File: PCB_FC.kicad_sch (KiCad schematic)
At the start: 20 parts, among them IC1 STM32F405RGT6, IC2 ICM-42670-P, U1 BMP388, U2 AMS1117-3.3, Y1 X32258MOB4SI

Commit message: Basic design of schametic done
1. Added folder for library
2. Added USB with termination resistors
3. Added Resistor network for bootstrapping and NRST
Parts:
- removed C5, C6: 10pF, Capacitor_SMD:C_0603_1608Metric_Pad1.08x0.95mm_HandSolder, symbol Device:C
- removed C7, C8, C9: C, Capacitor_SMD:C_0603_1608Metric_Pad1.08x0.95mm_HandSolder, symbol Device:C
- added C12, C15, C16, C17, C18, C19, C20, C21: 100nf, Capacitor_SMD:C_0603_1608Metric_Pad1.08x0.95mm_HandSolder, symbol Device:C
- added C13, C14: 10uf, Capacitor_SMD:C_0603_1608Metric_Pad1.08x0.95mm_HandSolder, symbol Device:C
- added D1: LED, symbol Device:LED
- added J1: 10104111-0001LF, Footprint:10104111-0001LF, symbol 10104111-0001LF:10104111-0001LF
- added R4: 4.7k, Resistor_SMD:R_0603_1608Metric_Pad0.98x0.95mm_HandSolder, symbol Device:R
- added R5: 10K, Resistor_SMD:R_0603_1608Metric_Pad0.98x0.95mm_HandSolder, symbol Device:R
- added R6: 10k, Resistor_SMD:R_0603_1608Metric_Pad0.98x0.95mm_HandSolder, symbol Device:R
- added R7, R8: 22R, Resistor_SMD:R_0603_1608Metric_Pad0.98x0.95mm_HandSolder, symbol Device:R
- added R9: 1k, Resistor_SMD:R_0603_1608Metric_Pad0.98x0.95mm_HandSolder, symbol Device:R
- added SW1: SW_SPST, Footprint:PTS636SKG25JSMTRLFS, symbol Switch:SW_SPST
- IC1: footprint KiCad:QFP50P1200X1200X160-64N -> Footprint:STM32F405RGT6
- IC2: footprint ICM-42670:ICM42670P -> Footprint:ICM-42670-P
- U1: footprint BMP388:PQFN50P200X200X80-10N -> Footprint:BMP388
- Y1: footprint X225:X32258MOB4SI -> Footprint:X32258MOB4SI
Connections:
- net VDD is gone; now on net +3.3V: IC1.13 (VDDA), IC1.19 (VDD_1), IC1.32 (VDD_2), IC1.48 (VDD_3), IC1.64 (VDD_4)
- net GND: now also Y1.2 (GND_1), C12.2, C13.2, C14.2, C15.2, C16.2, C17.2, C18.2, C19.2, C20.2, C21.2, J1.5, J1.6 (MP1), J1.7 (MP2), J1.8 (MP3), J1.9 (MP4), R6.1, R9.2, SW1.2 (B); no longer IC2.6 (GND)
- net I2C2_SCL: now also R1.2; no longer R1.1
- net I2C2_SDA: now also R4.2; no longer R2.1
- net LED_BLUE: now also D1.2 (A)
- net RCC_IN: now also Y1.3 (CRYSTAL_2); no longer Y1.1 (CRYSTAL_1)
- net RCC_OUT: now also IC1.6 (PH1), R3.2; no longer R3.1
- net at TP1.1, U2.3 (VI): now also C12.1, C13.1
- net SWDIO: now reaches IC1.46 (PA13)
- net SWCLK: now reaches IC1.49 (PA14)
- net at IC1.60 (BOOT0): now also R6.2
- net NRST: now reaches IC1.7 (NRST)
- net NRST: now also C21.1, R5.2, SW1.1 (A)
- net  OTG_FS_DM renamed OTG_FS_D-
- net OTG_FS_D-: now also R8.2
- net 3V3 renamed +3.3V
- net +3.3V: now also R1.1, R2.1, C14.1, C15.1, C16.1, C17.1, C18.1, C19.1, C20.1, R4.1, R5.1; no longer R1.2, R2.2
- net OTG_FS_DP renamed OTG_FS_D+
- net OTG_FS_D+: now also R7.2
- net PAD: no longer names the net of U1.6 (CSB)
- net PAD: now also R2.2
- new net: R3.1, Y1.1 (CRYSTAL_1)
- new net: D1.1 (K), R9.1
- new net +5V: J1.1
- new net D+: J1.3, R7.1
- new net D-: J1.2, R8.1
- no-connect marks 41 -> 38
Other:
- moved on the sheet: C1, C10, C11, C2, C3, C4, IC1, IC2, R1, R3, TP1, U1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

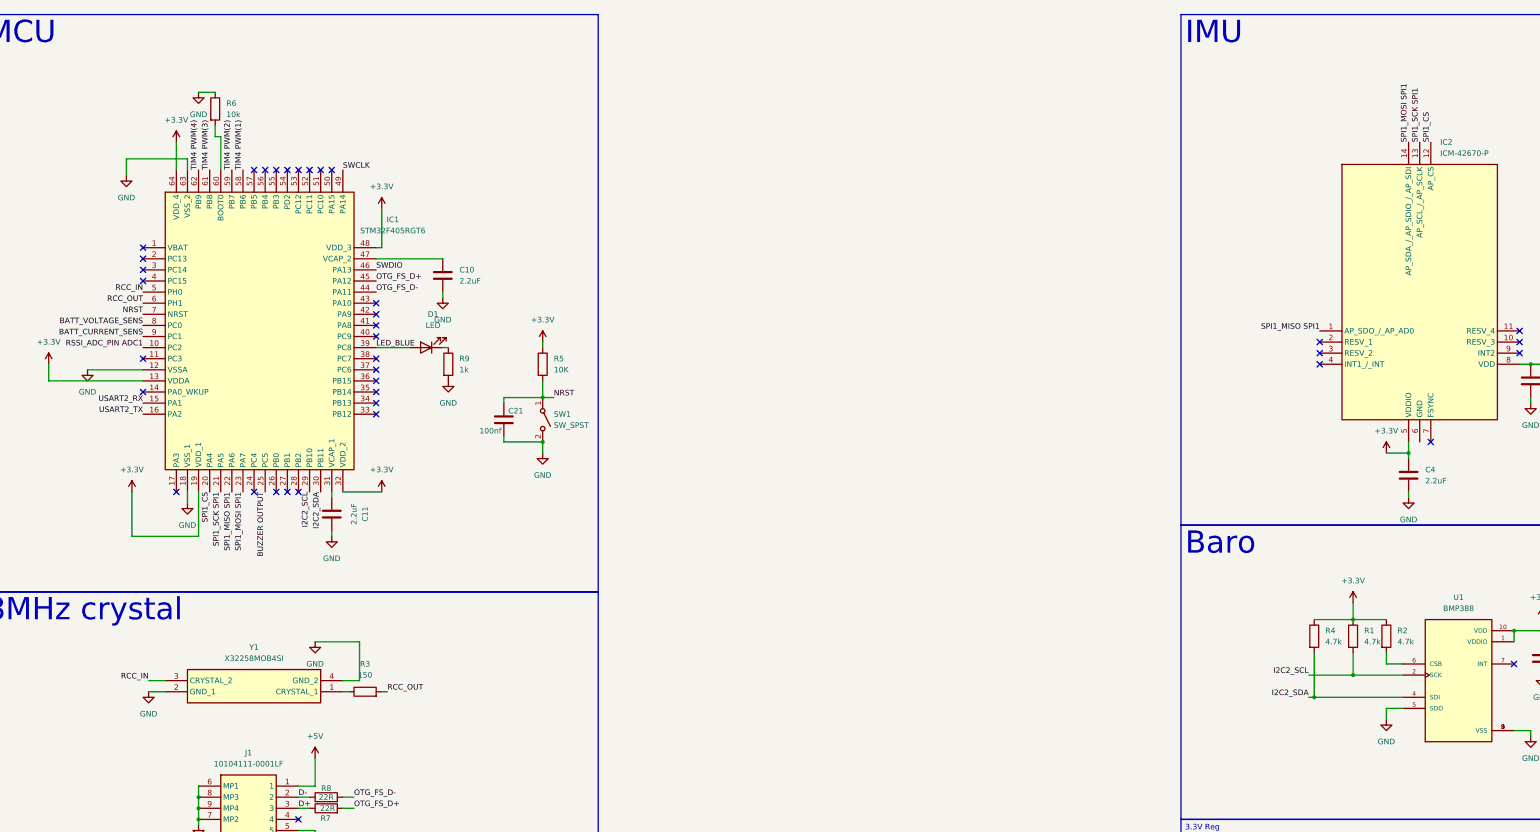
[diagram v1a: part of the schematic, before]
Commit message: Signal routing done
1. Routing for IMU
2. Differentially route pair for USB with termination resistor.
3. HSE crystal oscillator added.
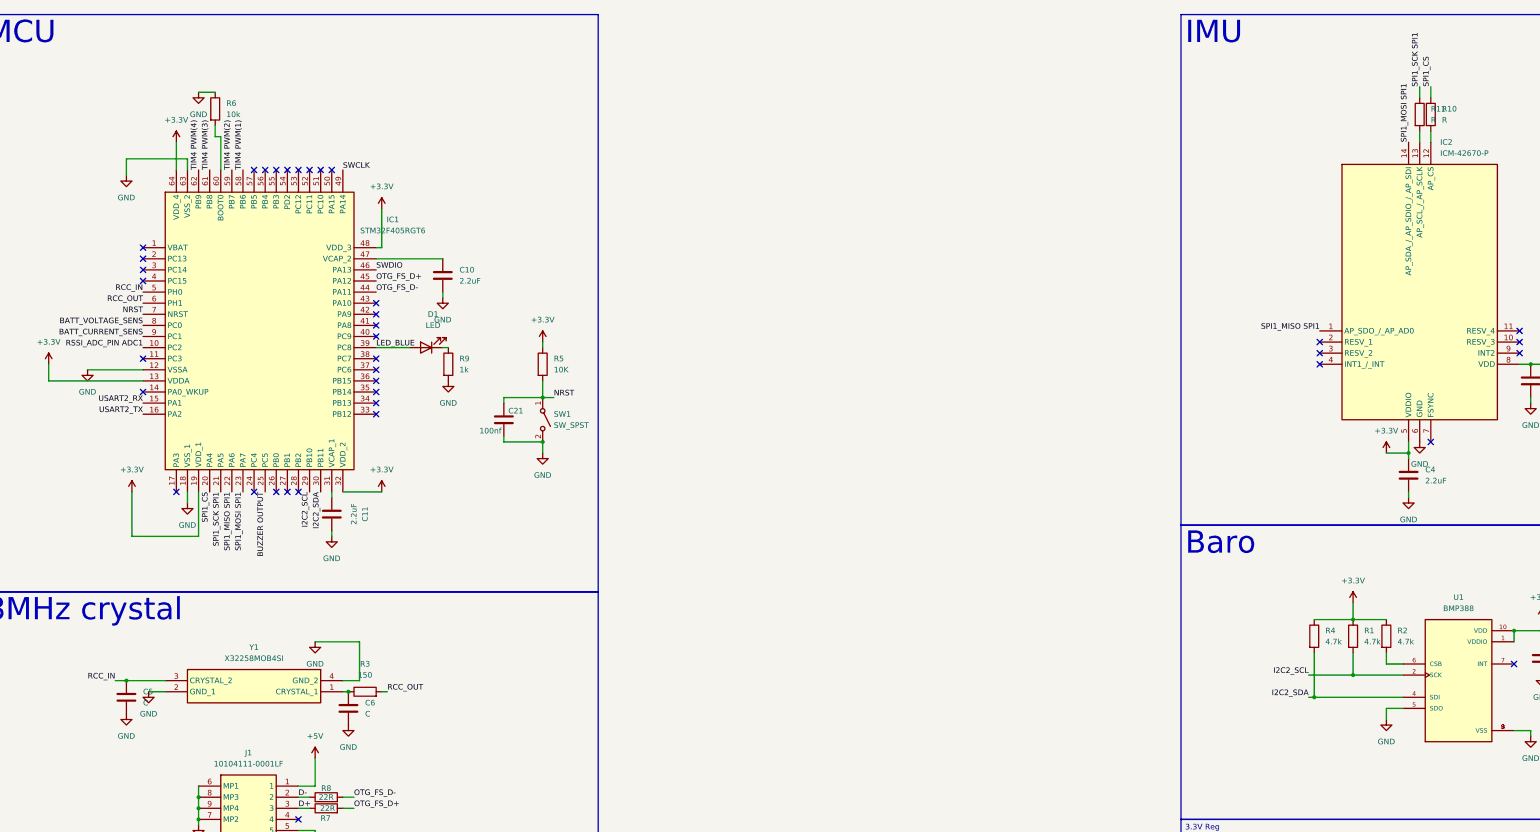
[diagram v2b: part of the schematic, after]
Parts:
- added C5, C6: C, Capacitor_SMD:C_0603_1608Metric_Pad1.08x0.95mm_HandSolder, symbol Device:C
- added R10, R11: R, Resistor_SMD:R_1206_3216Metric_Pad1.30x1.75mm_HandSolder, symbol Device:R
- C13, C14: footprint Capacitor_SMD:C_0603_1608Metric_Pad1.08x0.95mm_HandSolder -> Capacitor_SMD:C_0805_2012Metric_Pad1.18x1.45mm_HandSolder
- R7, R8: footprint Resistor_SMD:R_0603_1608Metric_Pad0.98x0.95mm_HandSolder -> Resistor_SMD:R_0402_1005Metric_Pad0.72x0.64mm_HandSolder
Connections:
- net GND: now also IC2.6 (GND), C5.2, C6.2
- net RCC_IN: now also C5.1
- net SPI1_CS: now also R10.1; no longer IC2.12 (AP_CS)
- net SPI1_SCK SPI1: now also R11.1; no longer IC2.13 (AP_SCL_/_AP_SCLK)
- net at R3.1, Y1.1 (CRYSTAL_1): now also C6.1
- new net: IC2.13 (AP_SCL_/_AP_SCLK), R11.2
- new net: IC2.12 (AP_CS), R10.2

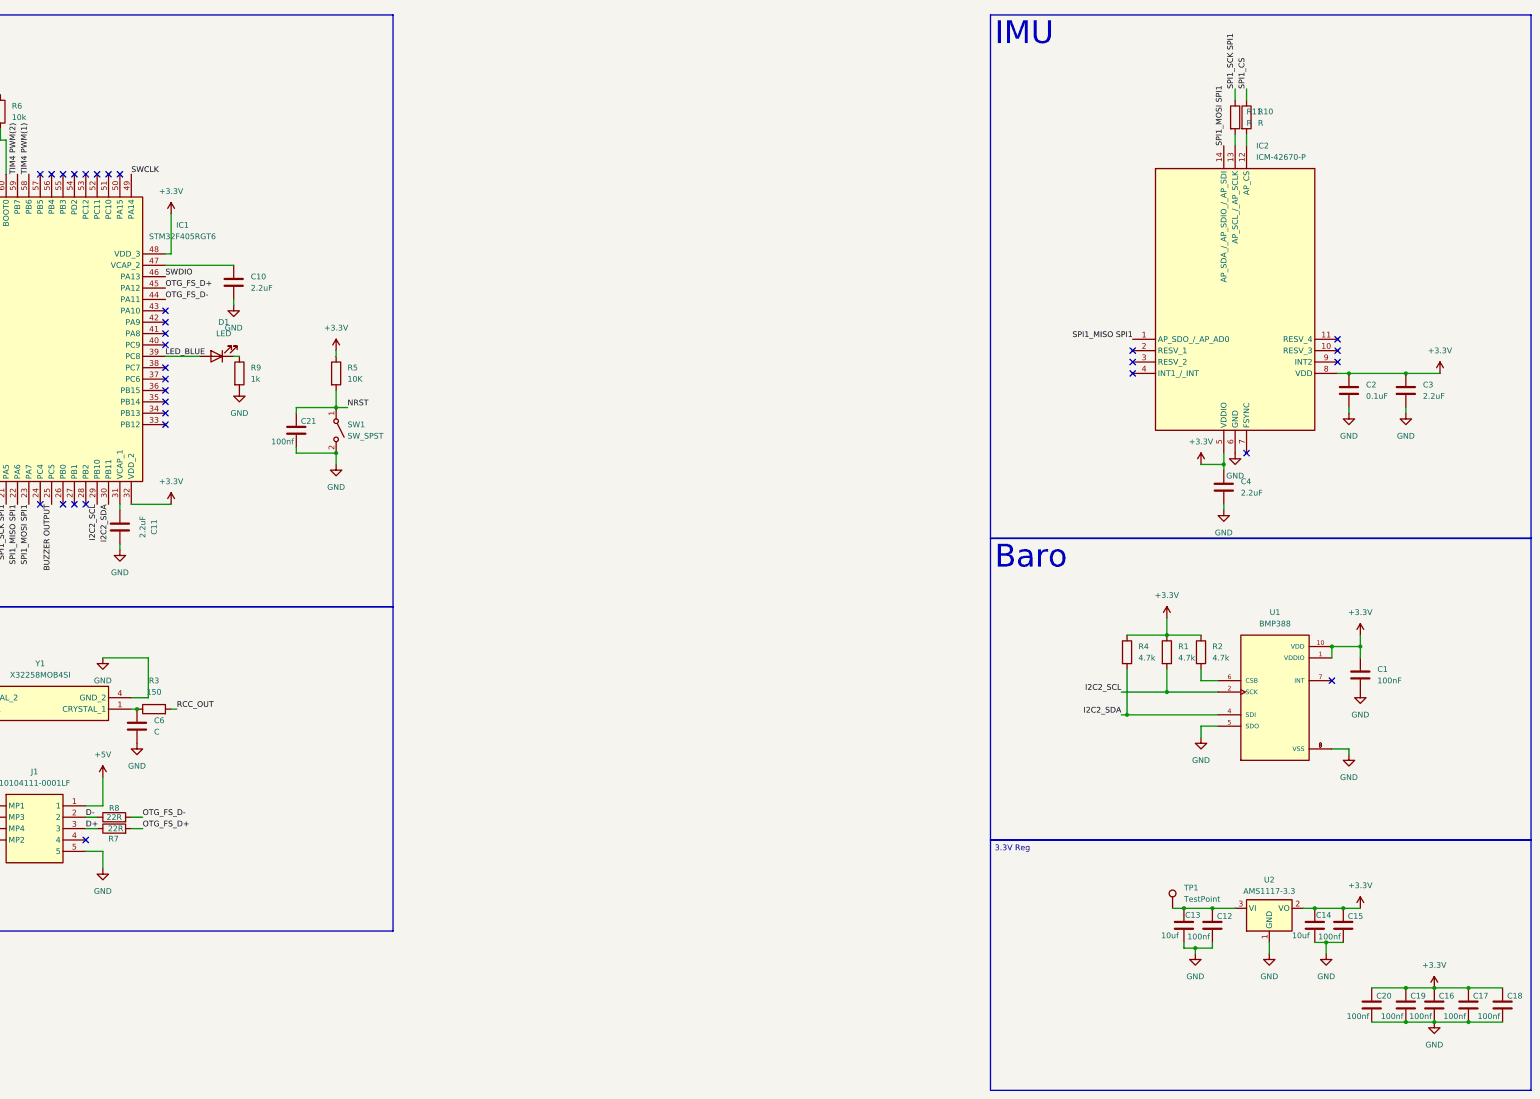
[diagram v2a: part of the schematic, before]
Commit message: PCB complete add logos
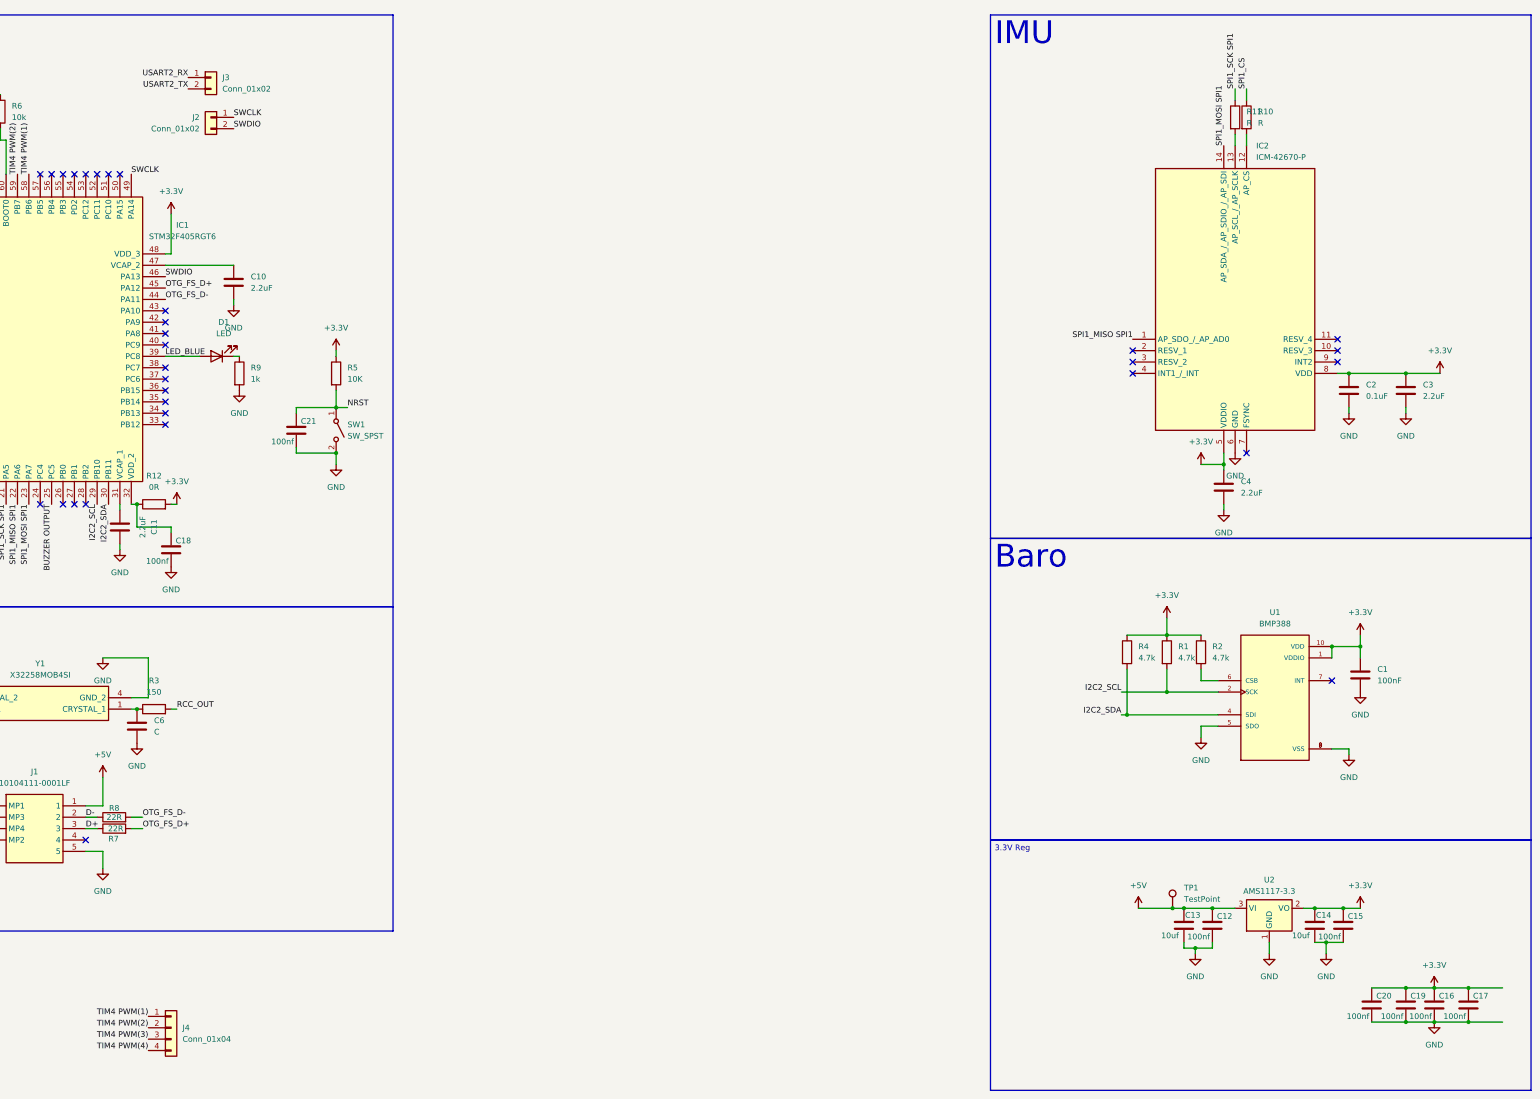
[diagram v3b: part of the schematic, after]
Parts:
- added J2, J3: Conn_01x02, Connector_PinHeader_2.54mm:PinHeader_1x02_P2.54mm_Vertical, symbol Connector_Generic:Conn_01x02
- added J4: Conn_01x04, symbol Connector_Generic:Conn_01x04
- added R12: 0R, Resistor_SMD:R_0603_1608Metric_Pad0.98x0.95mm_HandSolder, symbol Device:R
- D1: footprint (none) -> LED_SMD:LED_0402_1005Metric_Pad0.77x0.64mm_HandSolder
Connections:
- net +3.3V: now also R12.2; no longer C18.1, IC1.32 (VDD_2)
- net +5V: now also C12.1, C13.1, TP1.1, U2.3 (VI)
- net SWCLK: now also J2.1 (Pin_1)
- net SWDIO: now also J2.2 (Pin_2)
- net TIM4 PWM(1): now also J4.1 (Pin_1)
- net TIM4 PWM(2): now also J4.2 (Pin_2)
- net TIM4 PWM(3): now also J4.3 (Pin_3)
- net TIM4 PWM(4): now also J4.4 (Pin_4)
- net USART2_RX: now also J3.1 (Pin_1)
- net USART2_TX: now also J3.2 (Pin_2)
- new net: C18.1, IC1.32 (VDD_2), R12.1
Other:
- moved on the sheet: C18
